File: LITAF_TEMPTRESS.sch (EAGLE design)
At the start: 10 parts, among them T1 TMP117, T2 TMP117, U1 NTAG5_LINK_NTP53X2

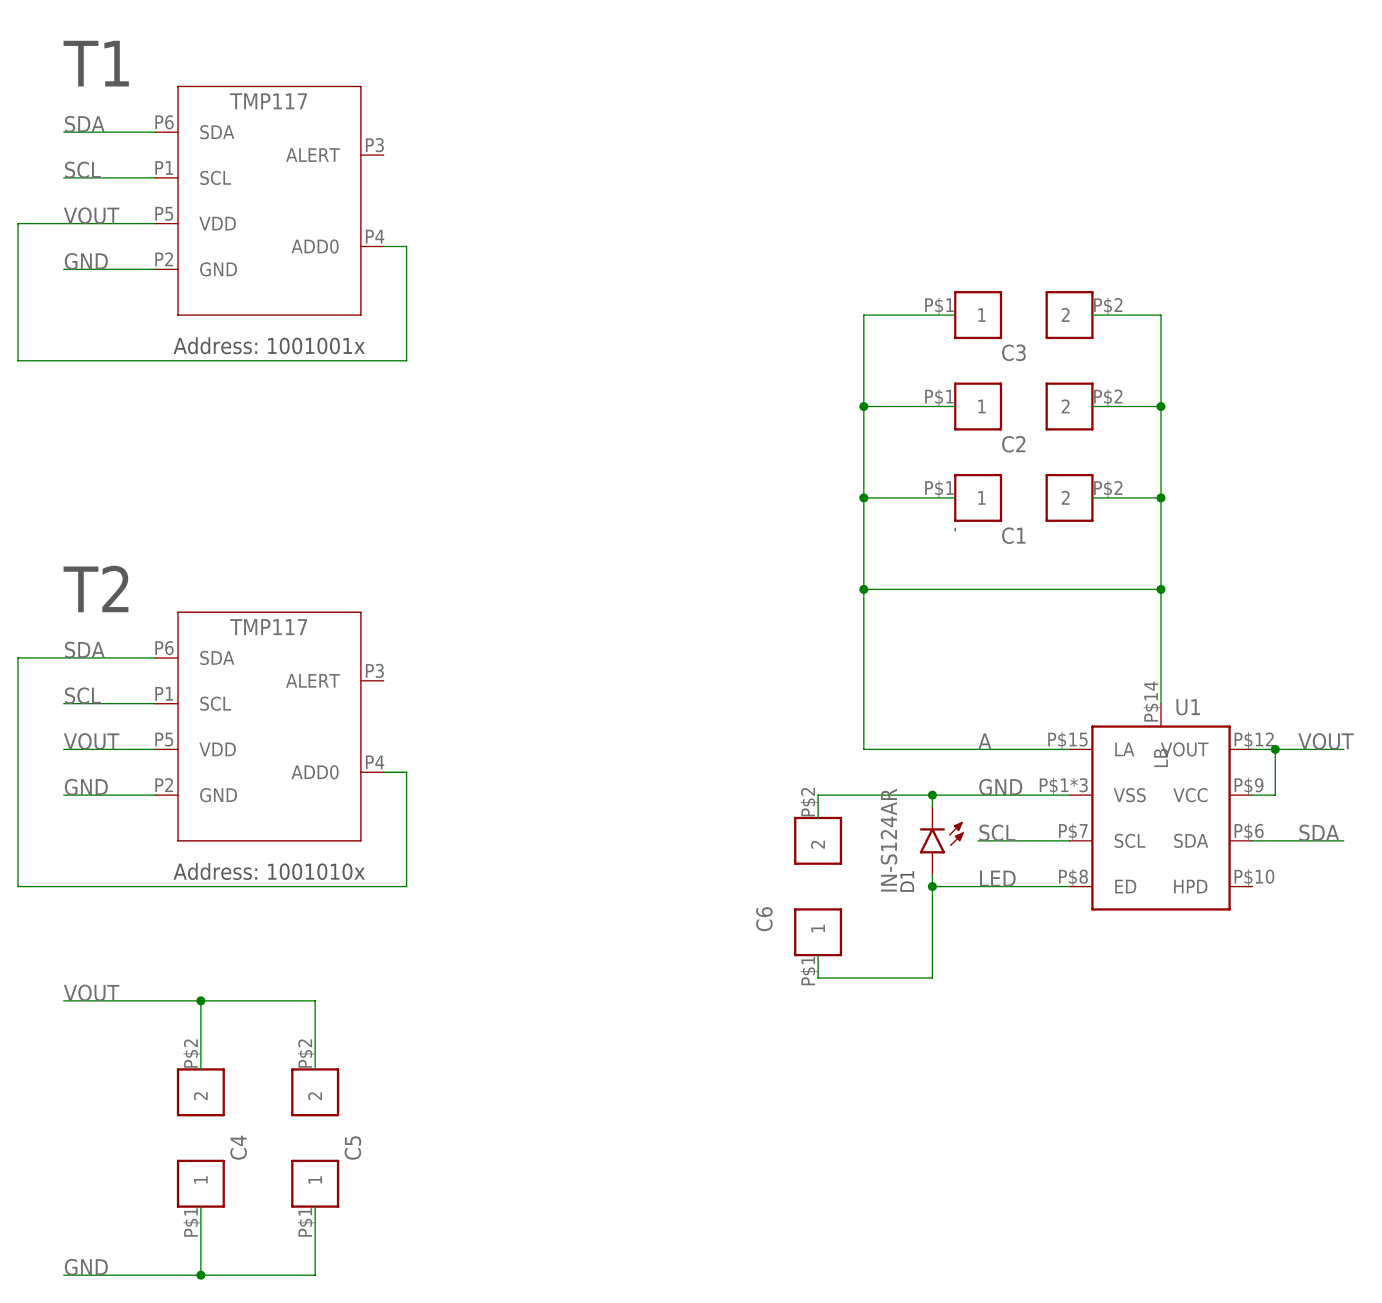
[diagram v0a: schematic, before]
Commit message: Added current limiting resistor for LED
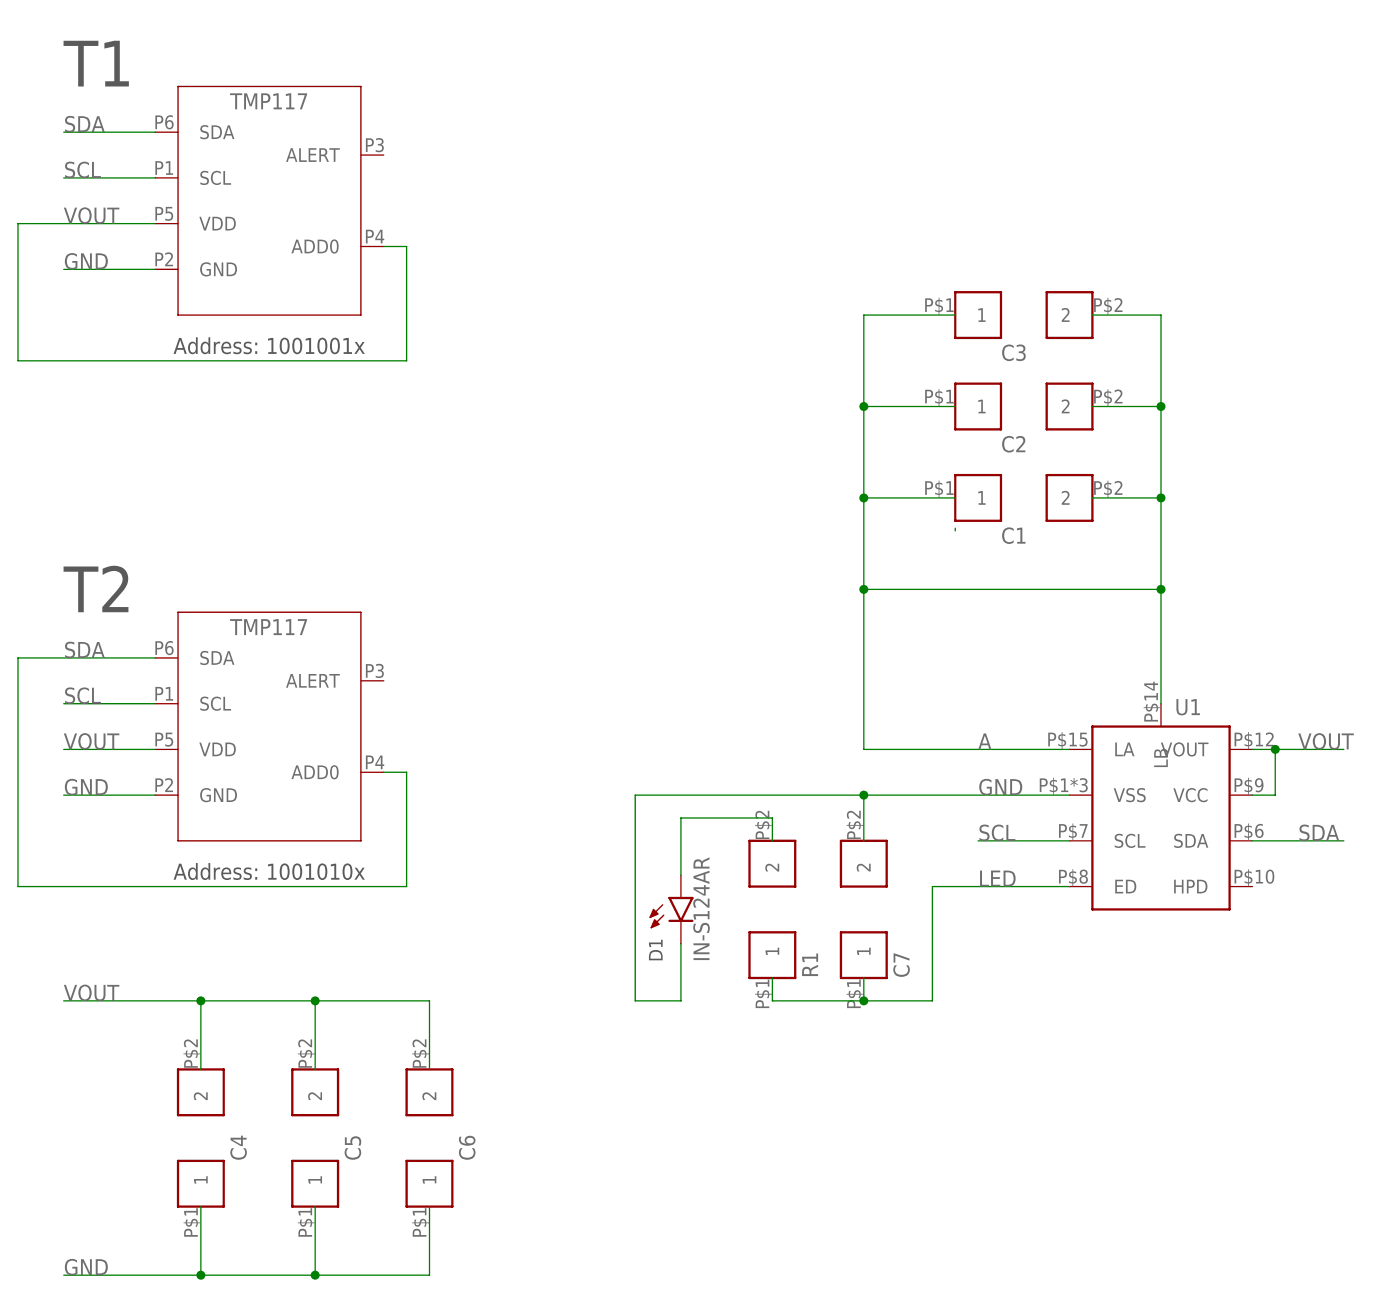
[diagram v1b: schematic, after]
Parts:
- added C7, R1: (no value), LITAF_TEMPTRESS:0402-CAP
- C5: device LITAF_TEMPTRESS:0603-CAP -> LITAF_TEMPTRESS:0402-CAP
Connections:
- new net N$1: D1.A, R1.2
- net GND: now also C6.1, C7.2; no longer C6.2
- net LED: now also C7.1, R1.1; no longer C6.1, D1.A
- net VOUT: now also C6.2
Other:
- moved on the sheet: C6
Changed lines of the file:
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@@
 <part name="D1" library="LITAF_TEMPTRESS" deviceset="IN-S124AR" device=""/>
 <part name="FRAME1" library="LITAF_TEMPTRESS" deviceset="A4L-LOC" device=""/>
+<part name="C5" library="LITAF_TEMPTRESS" deviceset="0402-CAP" device=""/>
 <part name="C4" library="LITAF_TEMPTRESS" deviceset="0603-CAP" device=""/>
-<part name="C5" library="LITAF_TEMPTRESS" deviceset="0603-CAP" device=""/>
-<part name="C6" library="LITAF_TEMPTRESS" deviceset="0402-CAP*?" device=""/>
+<part name="C7" library="LITAF_TEMPTRESS" deviceset="0402-CAP*?" device=""/>
+<part name="R1" library="LITAF_TEMPTRESS" deviceset="0402-CAP*?" device=""/>
+<part name="C6" library="LITAF_TEMPTRESS" deviceset="0402-CAP" device=""/>
 </parts>
 <sheets>
@@
 <text x="63.5" y="320.04" size="5.08" layer="97" align="top-left">T1</text>
 <text x="63.5" y="261.62" size="5.08" layer="97" align="top-left">T2</text>
-<text x="156.464" y="225.298" size="1.524" layer="97" rot="R90" align="top-left">D1</text>
+<text x="128.524" y="217.678" size="1.524" layer="97" rot="R90" align="top-left">D1</text>
 </plain>
 <instances>
@@
 <instance part="T1" gate="G$1" x="86.36" y="302.26" smashed="yes"/>
 <instance part="T2" gate="G$1" x="86.36" y="243.84" smashed="yes"/>
-<instance part="D1" gate="G$1" x="160.02" y="229.87" smashed="yes" rot="R180">
-<attribute name="VALUE" x="154.305" y="236.982" size="1.778" layer="96" rot="R270"/>
+<instance part="D1" gate="G$1" x="132.08" y="224.79" smashed="yes">
+<attribute name="VALUE" x="135.255" y="217.678" size="1.778" layer="96" rot="R90"/>
 </instance>
 <instance part="FRAME1" gate="G$1" x="40.64" y="147.32" smashed="yes">
@@
 <attribute name="SHEET" x="271.145" y="152.4" size="2.54" layer="94"/>
 </instance>
+<instance part="C5" gate="G$1" x="91.44" y="198.12" smashed="yes" rot="R90">
+<attribute name="NAME" x="96.52" y="195.58" size="1.778" layer="95" rot="R90"/>
+<attribute name="VALUE" x="87.884" y="193.04" size="1.27" layer="96" rot="R90"/>
+</instance>
 <instance part="C4" gate="G$1" x="78.74" y="198.12" smashed="yes" rot="R90">
 <attribute name="NAME" x="83.82" y="195.58" size="1.778" layer="95" rot="R90"/>
 <attribute name="VALUE" x="75.184" y="193.04" size="1.27" layer="96" rot="R90"/>
 </instance>
-<instance part="C5" gate="G$1" x="91.44" y="198.12" smashed="yes" rot="R90">
-<attribute name="NAME" x="96.52" y="195.58" size="1.778" layer="95" rot="R90"/>
-<attribute name="VALUE" x="87.884" y="193.04" size="1.27" layer="96" rot="R90"/>
-</instance>
-<instance part="C6" gate="G$1" x="147.32" y="226.06" smashed="yes" rot="R90">
-<attribute name="NAME" x="142.24" y="220.98" size="1.778" layer="95" rot="R90"/>
-<attribute name="VALUE" x="143.764" y="220.98" size="1.27" layer="96" rot="R90"/>
+<instance part="C7" gate="G$1" x="152.4" y="223.52" smashed="yes" rot="R90">
+<attribute name="NAME" x="157.48" y="215.9" size="1.778" layer="95" rot="R90"/>
+<attribute name="VALUE" x="148.844" y="218.44" size="1.27" layer="96" rot="R90"/>
+</instance>
+<instance part="R1" gate="G$1" x="142.24" y="223.52" smashed="yes" rot="R90">
+<attribute name="NAME" x="147.32" y="215.9" size="1.778" layer="95" rot="R90"/>
+<attribute name="VALUE" x="138.684" y="218.44" size="1.27" layer="96" rot="R90"/>
+</instance>
+<instance part="C6" gate="G$1" x="104.14" y="198.12" smashed="yes" rot="R90">
+<attribute name="NAME" x="109.22" y="195.58" size="1.778" layer="95" rot="R90"/>
+<attribute name="VALUE" x="100.584" y="193.04" size="1.27" layer="96" rot="R90"/>
 </instance>
 </instances>
@@
 <segment>
 <wire x1="78.74" y1="213.36" x2="63.5" y2="213.36" width="0.1524" layer="91"/>
+<pinref part="C5" gate="G$1" pin="2"/>
 <pinref part="C4" gate="G$1" pin="2"/>
+<wire x1="78.74" y1="213.36" x2="91.44" y2="213.36" width="0.1524" layer="91"/>
+<junction x="78.74" y="213.36"/>
+<pinref part="C6" gate="G$1" pin="2"/>
+<wire x1="91.44" y1="213.36" x2="104.14" y2="213.36" width="0.1524" layer="91"/>
+<wire x1="104.14" y1="213.36" x2="104.14" y2="205.74" width="0.1524" layer="91"/>
+<junction x="91.44" y="213.36"/>
 <wire x1="78.74" y1="213.36" x2="78.74" y2="205.74" width="0.1524" layer="91"/>
-<pinref part="C5" gate="G$1" pin="2"/>
-<wire x1="78.74" y1="213.36" x2="91.44" y2="213.36" width="0.1524" layer="91"/>
-<wire x1="91.44" y1="213.36" x2="91.44" y2="205.74" width="0.1524" layer="91"/>
-<junction x="78.74" y="213.36"/>
+<wire x1="91.44" y1="205.74" x2="91.44" y2="213.36" width="0.1524" layer="91"/>
 </segment>
 </net>
@@
 <segment>
 <pinref part="U1" gate="G$1" pin="VSS"/>
-<wire x1="175.26" y1="236.22" x2="160.02" y2="236.22" width="0.1524" layer="91"/>
 <label x="165.1" y="236.22" size="1.778" layer="95"/>
 <pinref part="D1" gate="G$1" pin="C"/>
-<wire x1="160.02" y1="236.22" x2="160.02" y2="234.95" width="0.1524" layer="91"/>
-<pinref part="C6" gate="G$1" pin="2"/>
-<wire x1="160.02" y1="236.22" x2="147.32" y2="236.22" width="0.1524" layer="91"/>
-<wire x1="147.32" y1="236.22" x2="147.32" y2="233.68" width="0.1524" layer="91"/>
-<junction x="160.02" y="236.22"/>
+<pinref part="C7" gate="G$1" pin="2"/>
+<wire x1="132.08" y1="219.71" x2="132.08" y2="213.36" width="0.1524" layer="91"/>
+<wire x1="132.08" y1="213.36" x2="127" y2="213.36" width="0.1524" layer="91"/>
+<wire x1="127" y1="213.36" x2="127" y2="236.22" width="0.1524" layer="91"/>
+<wire x1="127" y1="236.22" x2="152.4" y2="236.22" width="0.1524" layer="91"/>
+<wire x1="152.4" y1="236.22" x2="152.4" y2="231.14" width="0.1524" layer="91"/>
+<wire x1="152.4" y1="236.22" x2="175.26" y2="236.22" width="0.1524" layer="91"/>
+<junction x="152.4" y="236.22"/>
 </segment>
 <segment>
 <wire x1="78.74" y1="182.88" x2="63.5" y2="182.88" width="0.1524" layer="91"/>
+<pinref part="C5" gate="G$1" pin="1"/>
 <pinref part="C4" gate="G$1" pin="1"/>
-<wire x1="78.74" y1="182.88" x2="78.74" y2="190.5" width="0.1524" layer="91"/>
-<pinref part="C5" gate="G$1" pin="1"/>
 <wire x1="78.74" y1="182.88" x2="91.44" y2="182.88" width="0.1524" layer="91"/>
-<wire x1="91.44" y1="182.88" x2="91.44" y2="190.5" width="0.1524" layer="91"/>
 <junction x="78.74" y="182.88"/>
 <label x="63.5" y="182.88" size="1.778" layer="95"/>
+<pinref part="C6" gate="G$1" pin="1"/>
+<wire x1="91.44" y1="182.88" x2="104.14" y2="182.88" width="0.1524" layer="91"/>
+<wire x1="104.14" y1="182.88" x2="104.14" y2="190.5" width="0.1524" layer="91"/>
+<junction x="91.44" y="182.88"/>
+<wire x1="78.74" y1="190.5" x2="78.74" y2="182.88" width="0.1524" layer="91"/>
+<wire x1="91.44" y1="182.88" x2="91.44" y2="190.5" width="0.1524" layer="91"/>
 </segment>
 <segment>
@@
 <wire x1="175.26" y1="226.06" x2="160.02" y2="226.06" width="0.1524" layer="91"/>
 <label x="165.1" y="226.06" size="1.778" layer="95"/>
+<wire x1="160.02" y1="226.06" x2="160.02" y2="213.36" width="0.1524" layer="91"/>
+<pinref part="C7" gate="G$1" pin="1"/>
+<wire x1="152.4" y1="213.36" x2="152.4" y2="215.9" width="0.1524" layer="91"/>
+<wire x1="152.4" y1="213.36" x2="142.24" y2="213.36" width="0.1524" layer="91"/>
+<junction x="152.4" y="213.36"/>
+<pinref part="R1" gate="G$1" pin="1"/>
+<wire x1="142.24" y1="213.36" x2="142.24" y2="215.9" width="0.1524" layer="91"/>
+<wire x1="152.4" y1="213.36" x2="160.02" y2="213.36" width="0.1524" layer="91"/>
+</segment>
+</net>
+<net name="N$1" class="0">
+<segment>
 <pinref part="D1" gate="G$1" pin="A"/>
-<wire x1="160.02" y1="227.33" x2="160.02" y2="226.06" width="0.1524" layer="91"/>
-<wire x1="160.02" y1="226.06" x2="160.02" y2="215.9" width="0.1524" layer="91"/>
-<junction x="160.02" y="226.06"/>
-<pinref part="C6" gate="G$1" pin="1"/>
-<wire x1="160.02" y1="215.9" x2="147.32" y2="215.9" width="0.1524" layer="91"/>
-<wire x1="147.32" y1="215.9" x2="147.32" y2="218.44" width="0.1524" layer="91"/>
-</segment>
-</net>
+<pinref part="R1" gate="G$1" pin="2"/>
+<wire x1="142.24" y1="231.14" x2="142.24" y2="233.68" width="0.1524" layer="91"/>
+<wire x1="142.24" y1="233.68" x2="132.08" y2="233.68" width="0.1524" layer="91"/>
+<wire x1="132.08" y1="233.68" x2="132.08" y2="227.33" width="0.1524" layer="91"/>
+</segment>
+</net>
